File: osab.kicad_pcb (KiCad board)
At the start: 2 copper layers, 50 x 75 mm, 98 parts, among them CON1 TF-01A, CON2 PJ-3420-A-SMT, CON3 TYPE-C-31-M-12, Q1 BC847B, Q2 BC847B, SW1 PPP, SW10 RESET, SW11 Torch, SW2 VOL-, SW3 VOL+, SW4 CHAP-, SW5 CHAP+, SW6 OT/NT, SW7 BOOK-, SW8 BOOK+, SW9 XKB5858-Z-F, U1 VS1000, U2 ME6211C33M5G-N, U3 CAT25640, U4 TP4055, U5 MF5853CS, U6 PAM8302AAS, Y1 12MHz

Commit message: production: Routing tracks...
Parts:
- moved R4 12.2 mm to (130.8, 96.5), turned to -90 degrees
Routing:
- net Net-(R3-Pad1): track 2.17 -> 84.3 mm, vias 0 -> 6
- net Net-(R35-Pad2): track 0.00 -> 6.30 mm
- net Net-(R4-Pad1): track 45.6 -> 47.7 mm
- net Net-(R6-Pad1): track 51.9 -> 51.2 mm

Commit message: production: Routing tracks...
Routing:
- net Net-(C3-Pad1): track 10.3 -> 126.1 mm, vias 0 -> 6
- net Net-(R25-Pad2): track 44.9 -> 47.6 mm
- net Net-(R3-Pad1): track 84.3 -> 82.1 mm
- net Net-(R6-Pad1): track 51.2 -> 50.5 mm
- net Net-(R5-Pad1): track 82.3 -> 82.9 mm
- net Net-(CON2-Pad1): track 66.9 -> 67.4 mm

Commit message: production: Routing tracks...
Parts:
- moved R15 8.98 mm to (150.6, 92.8), turned to 90 degrees
- moved R14 8.75 mm to (149.1, 92.8), turned to -90 degrees
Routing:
- net Net-(R35-Pad2): track 6.30 -> 45.1 mm, vias 0 -> 2
- net Net-(R14-Pad2): track 0.00 -> 17.2 mm
- net Net-(R14-Pad1): track 0.00 -> 13.5 mm
- net GND: track 110.6 -> 117.9 mm, vias 45 -> 52
- net Net-(R8-Pad1): track 32.5 -> 38.8 mm, vias 2 -> 4
- net Net-(R2-Pad1): track 66.0 -> 72.3 mm
- net Net-(R33-Pad2): track 50.5 -> 51.4 mm

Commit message: production: Routing tracks...
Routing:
- net Net-(R35-Pad2): track 45.1 -> 117.2 mm, vias 2 -> 10
- net Net-(R7-Pad1): track 94.8 -> 90.0 mm
- net VCC: track 117.0 -> 115.2 mm
- net Net-(R24-Pad2): track 52.0 -> 52.7 mm

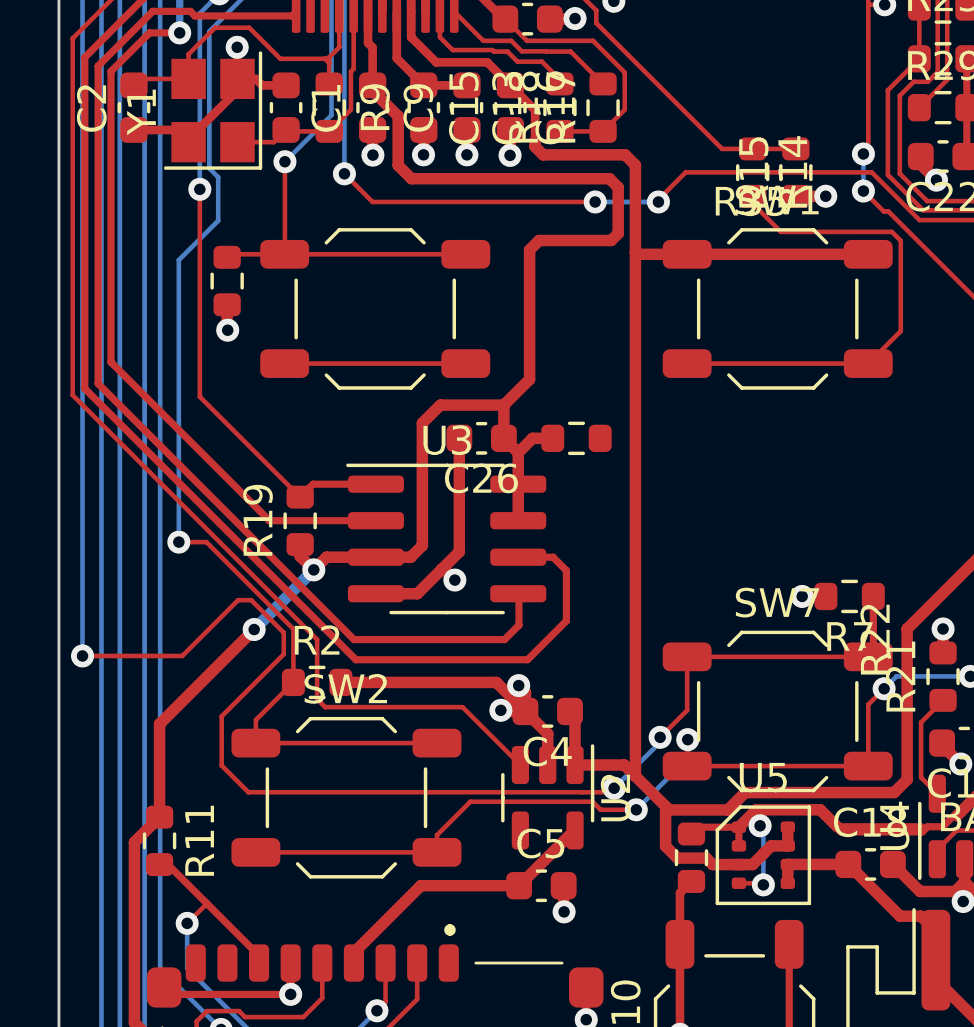
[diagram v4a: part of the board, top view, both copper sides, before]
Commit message: production: 0 unrouted
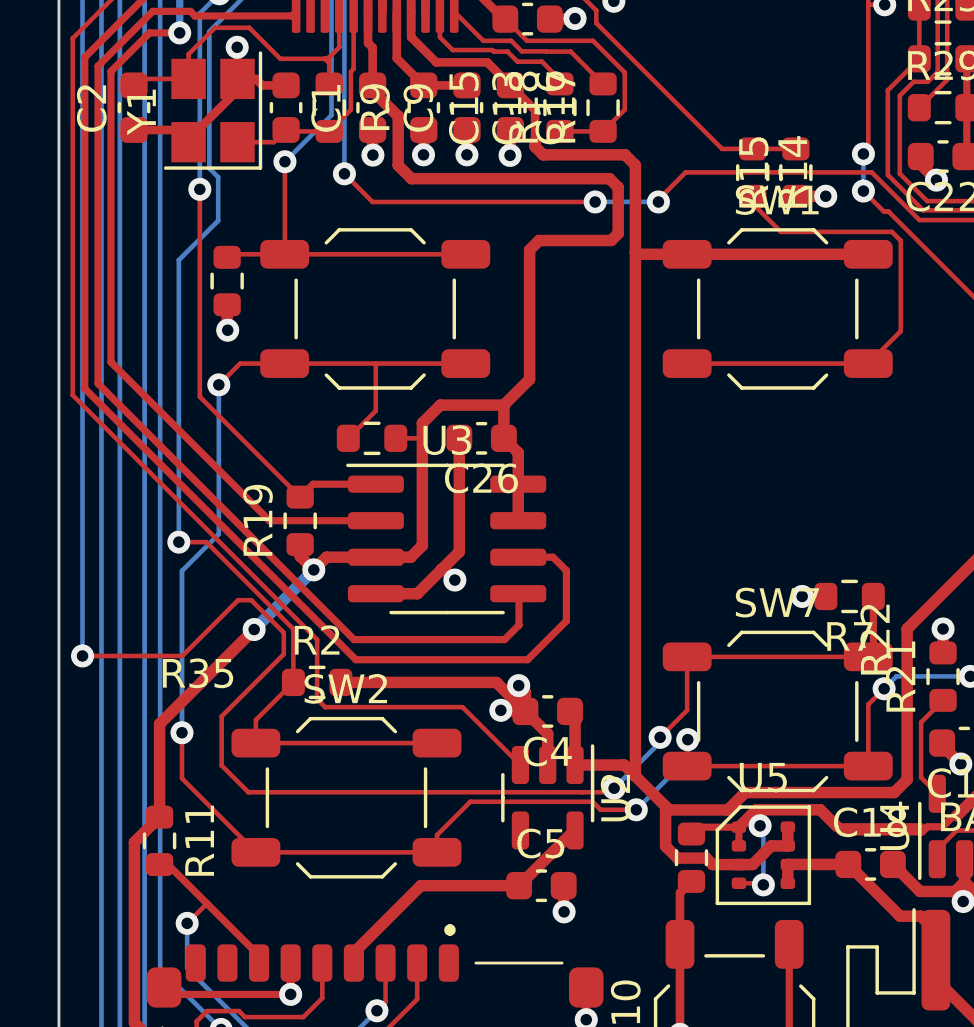
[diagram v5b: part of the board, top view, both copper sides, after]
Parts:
- moved R35 7.11 mm to (135.9, 102.0), turned to 180 degrees
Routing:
- net Net-(R35-Pad2): track 117.2 -> 140.6 mm, vias 10 -> 12
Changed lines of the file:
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@@
   )
   (footprint "Resistor_SMD:R_0603_1608Metric" (layer "F.Cu")
-    (at 143 102)
+    (at 135.89 102 180)
     (descr "Resistor SMD 0603 (1608 Metric), square (rectangular) end terminal, IPC_7351 nominal, (Body size source: IPC-SM-782 page 72, https://www.pcb-3d.com/wordpress/wp-content/uploads/ipc-sm-782a_amendment_1_and_2.pdf), generated with kicad-footprint-generator")
     (tags "resistor")
@@
     (fp_line (start -0.8 -0.4125) (end 0.8 -0.4125) (layer "F.Fab") (width 0.1))
     (fp_line (start 0.8 -0.4125) (end 0.8 0.4125) (layer "F.Fab") (width 0.1))
-    (pad "1" smd roundrect (at -0.825 0) (size 0.8 0.95) (layers "F.Cu" "F.Paste" "F.Mask") (roundrect_rratio 0.25)
+    (pad "1" smd roundrect (at -0.825 0 180) (size 0.8 0.95) (layers "F.Cu" "F.Paste" "F.Mask") (roundrect_rratio 0.25)
       (net 8 "VDD") (pintype "passive"))
-    (pad "2" smd roundrect (at 0.825 0) (size 0.8 0.95) (layers "F.Cu" "F.Paste" "F.Mask") (roundrect_rratio 0.25)
+    (pad "2" smd roundrect (at 0.825 0 180) (size 0.8 0.95) (layers "F.Cu" "F.Paste" "F.Mask") (roundrect_rratio 0.25)
       (net 66 "Net-(R35-Pad2)") (pintype "passive"))
     (model "${KICAD6_3DMODEL_DIR}/Resistor_SMD.3dshapes/R_0603_1608Metric.wrl"
@@
   (segment (start 137.64 101.47) (end 138.265 100.845) (width 0.4) (layer "F.Cu") (net 8))
   (segment (start 141.7 95.12) (end 144.21 95.12) (width 0.4) (layer "F.Cu") (net 8))
+  (segment (start 137.64 102.02) (end 137.64 101.47) (width 0.4) (layer "F.Cu") (net 8))
   (segment (start 140.975 104.865) (end 140.975 102.5) (width 0.4) (layer "F.Cu") (net 8))
   (segment (start 140.475 102) (end 140.475 100.845) (width 0.4) (layer "F.Cu") (net 8))
@@
   (segment (start 134.82 77.09) (end 135.75 77.09) (width 0.16) (layer "F.Cu") (net 8))
   (segment (start 136.8 90.8) (end 135.91 89.91) (width 0.4) (layer "F.Cu") (net 8))
-  (segment (start 137.64 105.73) (end 137.64 101.47) (width 0.4) (layer "F.Cu") (net 8))
   (segment (start 141.37 95.45) (end 141.7 95.12) (width 0.4) (layer "F.Cu") (net 8))
   (segment (start 134.57 82.26) (end 133.58 83.25) (width 0.3) (layer "F.Cu") (net 8))
@@
   (segment (start 128.5 115.175) (end 128.5 111.93) (width 0.4) (layer "F.Cu") (net 8))
   (segment (start 133.58 83.25) (end 131.8375 83.25) (width 0.3) (layer "F.Cu") (net 8))
+  (segment (start 136.715 102) (end 137.62 102) (width 0.16) (layer "F.Cu") (net 8))
   (segment (start 136.8 92.51) (end 136.8 90.8) (width 0.4) (layer "F.Cu") (net 8))
   (segment (start 134.1 75.46) (end 134.1 76.37) (width 0.16) (layer "F.Cu") (net 8))
-  (segment (start 141.475 102) (end 140.975 102.5) (width 0.4) (layer "F.Cu") (net 8))
   (segment (start 132.9 73.29) (end 132.9 72.325) (width 0.16) (layer "F.Cu") (net 8))
   (segment (start 135.64 83.33) (end 134.57 82.26) (width 0.3) (layer "F.Cu") (net 8))
@@
   (segment (start 140.475 100.845) (end 141.37 99.95) (width 0.4) (layer "F.Cu") (net 8))
   (segment (start 134.1 76.37) (end 134.82 77.09) (width 0.16) (layer "F.Cu") (net 8))
+  (segment (start 137.64 105.73) (end 137.64 102.02) (width 0.4) (layer "F.Cu") (net 8))
   (segment (start 133.39 106.101104) (end 133.864448 106.575552) (width 0.4) (layer "F.Cu") (net 8))
   (segment (start 133.864448 106.575552) (end 134.305 106.135) (width 0.4) (layer "F.Cu") (net 8))
@@
   (segment (start 137.26 92.97) (end 136.8 92.51) (width 0.4) (layer "F.Cu") (net 8))
   (segment (start 130.5 83.25) (end 130 83.75) (width 0.3) (layer "F.Cu") (net 8))
+  (segment (start 137.62 102) (end 137.64 102.02) (width 0.16) (layer "F.Cu") (net 8))
   (segment (start 135.75 78.8375) (end 135.75 81.08) (width 0.3) (layer "F.Cu") (net 8))
   (segment (start 135.75 86.02) (end 135.64 85.91) (width 0.3) (layer "F.Cu") (net 8))
@@
   (segment (start 144.21 95.12) (end 144.45 94.88) (width 0.4) (layer "F.Cu") (net 8))
   (segment (start 135.75 87.1625) (end 135.75 86.02) (width 0.3) (layer "F.Cu") (net 8))
-  (segment (start 142.175 102) (end 141.475 102) (width 0.4) (layer "F.Cu") (net 8))
   (segment (start 133.39 105.695) (end 133.39 106.101104) (width 0.4) (layer "F.Cu") (net 8))
   (via (at 131.79 108.65) (size 0.8) (drill 0.4) (layers "F.Cu" "B.Cu") (net 8))
@@
   (segment (start 130.9 68.7125) (end 130.9 70.675) (width 0.25) (layer "F.Cu") (net 65))
   (segment (start 139.31 114.64) (end 143.56 114.64) (width 0.16) (layer "F.Cu") (net 66))
+  (segment (start 131.3 99.4) (end 132.85 99.4) (width 0.16) (layer "F.Cu") (net 66))
   (segment (start 157.47 81.94) (end 156.91 82.5) (width 0.16) (layer "F.Cu") (net 66))
   (segment (start 146.85 113.4) (end 153.15 113.4) (width 0.16) (layer "F.Cu") (net 66))
@@
   (segment (start 163.3 98.33) (end 166.08 98.33) (width 0.16) (layer "F.Cu") (net 66))
   (segment (start 161.85 116.4) (end 161.85 114.96) (width 0.16) (layer "F.Cu") (net 66))
+  (segment (start 132.85 99.4) (end 136.02 99.4) (width 0.16) (layer "F.Cu") (net 66))
+  (segment (start 136.02 99.4) (end 139.15 99.4) (width 0.16) (layer "F.Cu") (net 66))
+  (segment (start 130.56 100.14) (end 131.3 99.4) (width 0.16) (layer "F.Cu") (net 66))
   (segment (start 157.19 110.3) (end 157.17 110.28) (width 0.16) (layer "F.Cu") (net 66))
   (segment (start 152.98 92.11) (end 153.15 91.94) (width 0.16) (layer "F.Cu") (net 66))
   (segment (start 153.85 94.11) (end 153.69 94.11) (width 0.16) (layer "F.Cu") (net 66))
   (segment (start 153.15 111.26) (end 153.15 113.4) (width 0.16) (layer "F.Cu") (net 66))
+  (segment (start 135.065 102) (end 136.02 101.045) (width 0.16) (layer "F.Cu") (net 66))
   (segment (start 161.68 98.34) (end 158.08 98.34) (width 0.16) (layer "F.Cu") (net 66))
+  (segment (start 131.85 116.4) (end 129.28 113.83) (width 0.16) (layer "F.Cu") (net 66))
   (segment (start 158.08 98.34) (end 153.85 94.11) (width 0.16) (layer "F.Cu") (net 66))
   (segment (start 166.08 98.33) (end 167.15 99.4) (width 0.16) (layer "F.Cu") (net 66))
@@
   (segment (start 153.16 86.92) (end 153.15 86.91) (width 0.16) (layer "F.Cu") (net 66))
   (segment (start 143.56 114.64) (end 143.84 114.92) (width 0.16) (layer "F.Cu") (net 66))
+  (segment (start 136.02 101.045) (end 136.02 99.4) (width 0.16) (layer "F.Cu") (net 66))
   (segment (start 161.85 82.4) (end 168.15 82.4) (width 0.16) (layer "F.Cu") (net 66))
   (segment (start 161.68 98.57) (end 161.68 98.34) (width 0.16) (layer "F.Cu") (net 66))
   (segment (start 160.85 99.4) (end 161.68 98.57) (width 0.16) (layer "F.Cu") (net 66))
-  (segment (start 132.85 99.4) (end 139.15 99.4) (width 0.16) (layer "F.Cu") (net 66))
   (segment (start 146.85 112.5) (end 146.85 113.4) (width 0.16) (layer "F.Cu") (net 66))
   (segment (start 153.7 110.71) (end 153.15 111.26) (width 0.16) (layer "F.Cu") (net 66))
   (segment (start 138.15 115.8) (end 139.31 114.64) (width 0.16) (layer "F.Cu") (net 66))
   (segment (start 161.09 82.4) (end 160.63 81.94) (width 0.16) (layer "F.Cu") (net 66))
+  (segment (start 129.28 113.83) (end 129.28 112.24) (width 0.16) (layer "F.Cu") (net 66))
   (segment (start 153.15 91.94) (end 153.15 86.91) (width 0.16) (layer "F.Cu") (net 66))
   (segment (start 157.17 110.28) (end 156.7 110.28) (width 0.16) (layer "F.Cu") (net 66))
@@
   (via (at 161.68 98.34) (size 0.8) (drill 0.4) (layers "F.Cu" "B.Cu") (net 66))
   (via (at 156.91 82.5) (size 0.8) (drill 0.4) (layers "F.Cu" "B.Cu") (net 66))
+  (via (at 130.56 100.14) (size 0.8) (drill 0.4) (layers "F.Cu" "B.Cu") (net 66))
+  (via (at 129.28 112.24) (size 0.8) (drill 0.4) (layers "F.Cu" "B.Cu") (net 66))
   (via (at 153.7 110.71) (size 0.8) (drill 0.4) (layers "F.Cu" "B.Cu") (net 66))
   (segment (start 154.13 110.28) (end 153.7 110.71) (width 0.16) (layer "B.Cu") (net 66))
@@
   (segment (start 156.91 82.5) (end 156.91 83.73) (width 0.16) (layer "B.Cu") (net 66))
   (segment (start 145.08 114.92) (end 146.87 113.13) (width 0.16) (layer "B.Cu") (net 66))
+  (segment (start 130.56 105.33) (end 130.56 100.14) (width 0.16) (layer "B.Cu") (net 66))
+  (segment (start 129.28 106.61) (end 130.56 105.33) (width 0.16) (layer "B.Cu") (net 66))
   (segment (start 146.87 113.13) (end 146.87 112.48) (width 0.16) (layer "B.Cu") (net 66))
+  (segment (start 129.28 112.24) (end 129.28 106.61) (width 0.16) (layer "B.Cu") (net 66))
   (segment (start 156.91 83.73) (end 153.72 86.92) (width 0.16) (layer "B.Cu") (net 66))
   (segment (start 163.29 98.34) (end 163.3 98.33) (width 0.16) (layer "B.Cu") (net 66))

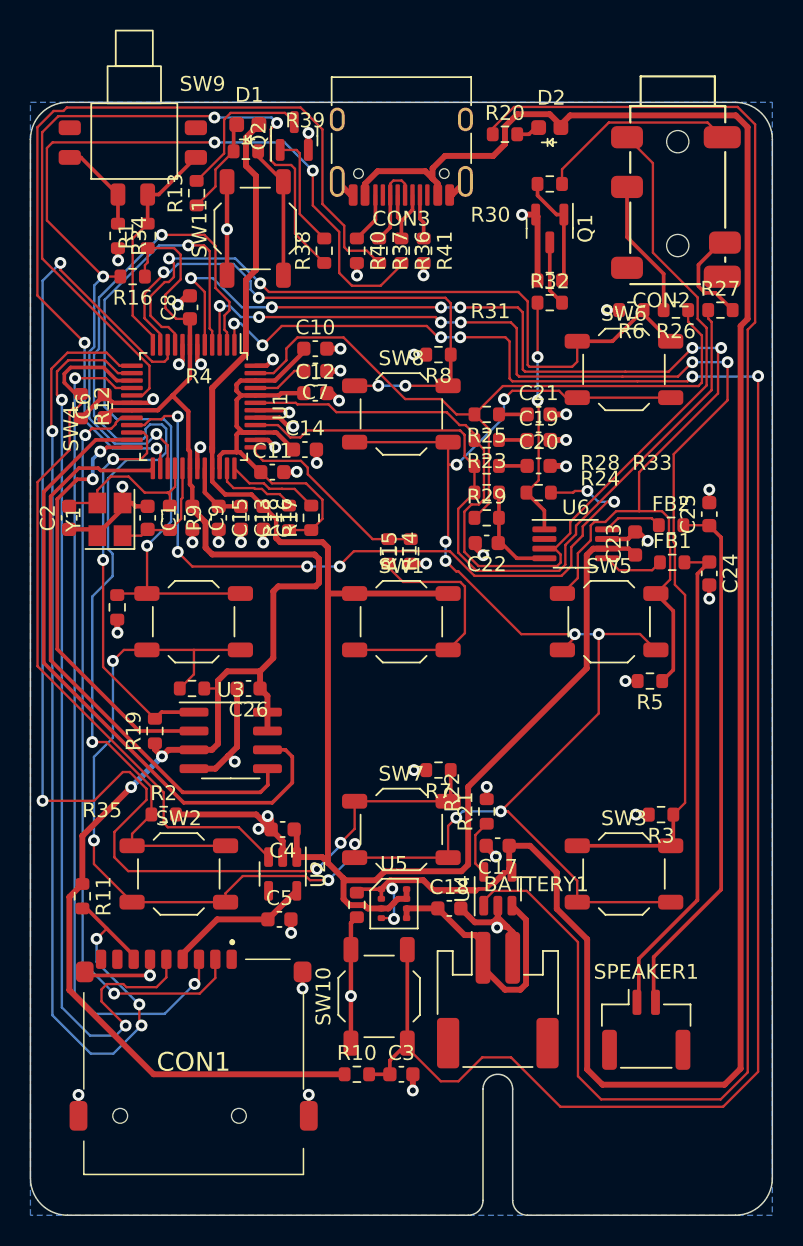
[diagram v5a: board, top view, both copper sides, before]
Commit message: production: DRC fixes
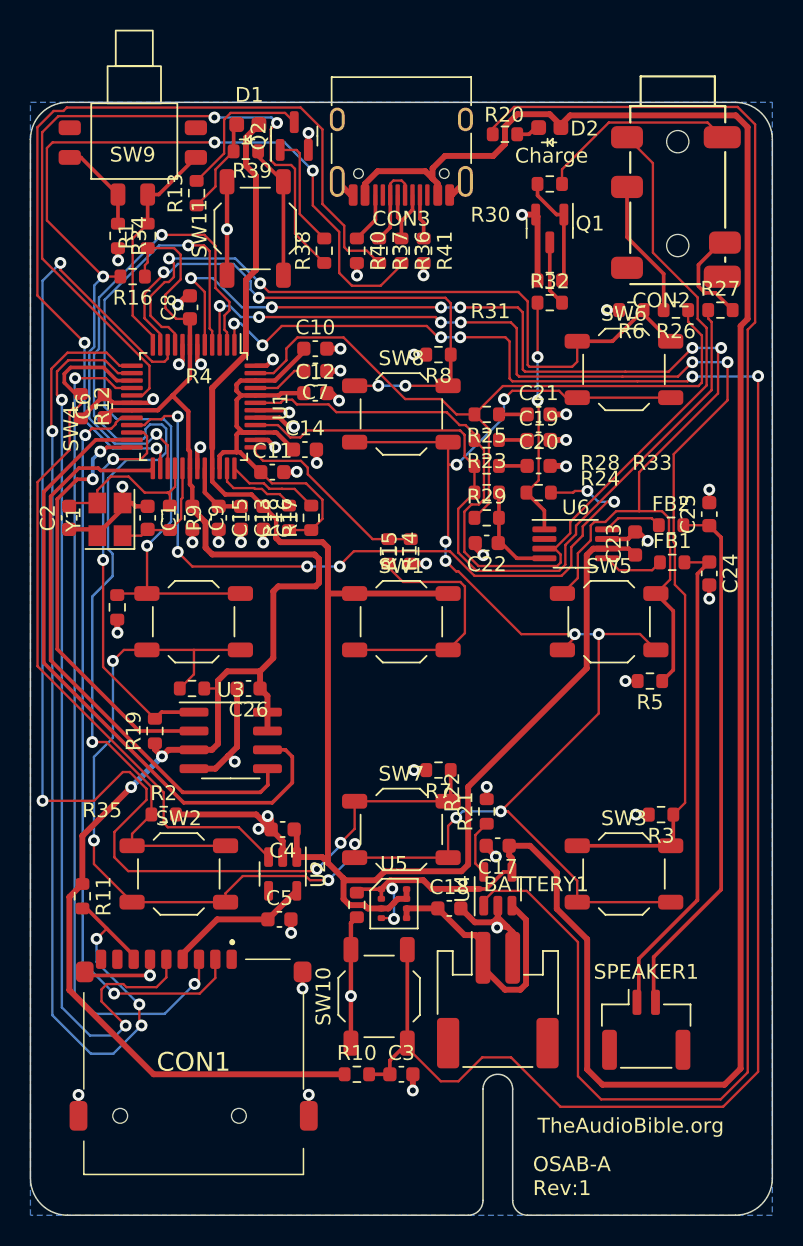
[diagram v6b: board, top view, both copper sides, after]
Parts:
- D2: value Charge LED -> Charge
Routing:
- net Net-(C17-Pad1): track 147.1 -> 142.4 mm
- net AVDD: track 33.9 -> 33.3 mm
- net Net-(C7-Pad2): track 4.26 -> 3.74 mm
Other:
- board text added: "OSAB-A Rev:1"
- board text added: "TheAudioBible.org"

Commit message: production: Added LCSC references
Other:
- board text added: "OSAB model A Rev 1"
- board text removed: "OSAB-A Rev:1"
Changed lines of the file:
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@@
   (paper "A4")
   (title_block
-    (title "OSAB-A-1.0")
+    (title "OSAB model A")
     (date "2022-06-02")
     (rev "1")
@@
     (property "Sheetname" "")
     (attr smd)
-    (fp_text reference "Q2" (at 0 -2.4 90) (layer "F.SilkS")
+    (fp_text reference "Q2" (at 1.45 1.32 180) (layer "F.SilkS")
       (effects (font (size 1 1) (thickness 0.15)))
     )
@@
     (property "Sheetname" "")
     (attr smd)
-    (fp_text reference "R34" (at 0 -1.43 90) (layer "F.SilkS")
+    (fp_text reference "R34" (at 0.33 1.22 90) (layer "F.SilkS")
       (effects (font (size 1 1) (thickness 0.15)))
     )
-    (fp_text value "10k" (at 0 1.43 90) (layer "F.Fab")
+    (fp_text value "10k" (at 0.04 0 90) (layer "F.Fab")
       (effects (font (size 1 1) (thickness 0.15)))
     )
@@
     (property "Sheetname" "")
     (attr smd)
-    (fp_text reference "R39" (at 0.42 1.31) (layer "F.SilkS")
+    (fp_text reference "R39" (at 0.61 1.32) (layer "F.SilkS")
       (effects (font (size 1 1) (thickness 0.15)))
     )
@@
     (property "Sheetname" "")
     (attr smd)
-    (fp_text reference "SW11" (at 0 -3.75 90) (layer "F.SilkS")
+    (fp_text reference "SW11" (at -0.01 0.13) (layer "F.SilkS")
       (effects (font (size 1 1) (thickness 0.15)))
     )
@@
     (property "Sheetname" "")
     (attr smd)
-    (fp_text reference "R13" (at 0 -1.43 90) (layer "F.SilkS")
+    (fp_text reference "R13" (at -0.1 -1.88 180) (layer "F.SilkS")
       (effects (font (size 1 1) (thickness 0.15)))
     )
@@
     (property "Sheetname" "")
     (attr smd)
-    (fp_text reference "R1" (at 0 -1.43 90) (layer "F.SilkS")
+    (fp_text reference "R1" (at 1.25 1.48 90) (layer "F.SilkS")
       (effects (font (size 1 1) (thickness 0.15)))
     )
-    (fp_text value "100k" (at 0 1.43 90) (layer "F.Fab")
+    (fp_text value "100k" (at -0.31 -0.02 90) (layer "F.Fab")
       (effects (font (size 1 1) (thickness 0.15)))
     )
@@
     (property "Sheetname" "")
     (attr smd)
-    (fp_text reference "D1" (at 0.1 -2 unlocked) (layer "F.SilkS")
+    (fp_text reference "D1" (at -2.08 -0.87 unlocked) (layer "F.SilkS")
       (effects (font (size 1 1) (thickness 0.15)))
     )
@@
       (effects (font (size 1 1) (thickness 0.15)))
     )
-    (fp_text value "XKB5858-Z-F" (at -0.1 5.4 unlocked) (layer "F.Fab")
+    (fp_text value "XKB5858-Z-F" (at -0.33 0.1975 unlocked) (layer "F.Fab")
       (effects (font (size 1 1) (thickness 0.15)))
     )
@@
   (gr_rect locked (start 125 62.5) (end 126.5 137.5) (layer "F.CrtYd") (width 0.05) (fill none))
   (gr_rect locked (start 175 62.5) (end 173.5 137.5) (layer "F.CrtYd") (width 0.05) (fill none))
-  (gr_text "OSAB-A\nRev:1" (at 158.86 134.87) (layer "F.SilkS")
+  (gr_text "OSAB\nmodel A\nRev 1" (at 147.18 133.47) (layer "F.SilkS")
     (effects (font (size 1 1) (thickness 0.15)) (justify left))
   )
-  (gr_text "TheAudioBible.org" (at 165.46 131.47) (layer "F.SilkS")
+  (gr_text "TheAudioBible.org" (at 165.19 133.55) (layer "F.SilkS")
     (effects (font (size 1 1) (thickness 0.15)))
   )

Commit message: production: Text layout
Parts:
- D2: value Charge -> Charge LED
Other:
- board text added: "+"
- board text added: "-"
- board text added: "OSAB model A rev 1"
- board text removed: "OSAB model A Rev 1"
